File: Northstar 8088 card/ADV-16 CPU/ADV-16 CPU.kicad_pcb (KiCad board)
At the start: 2 copper layers, 228.1 x 165.3 mm, 111 parts, among them J1 Power In, J2 Conn_01x16_Socket, J3 Conn_01x18_Socket, P1 northstar card edge, Q1 2N3904, U1 74LS175, U10 74LS155, U11 74LS373, U12 8088-2, U13 74LS00, U14 74LS04, U15 74LS393, U16 74S08, U17 8284, U18 74LS258, U19 74LS174, U2 74S112, U20 74LS03, U21 74LS153, U22 74LS74, U23 74S00, U24 74LS393, U25 74LS244, U26 74LS258, U27 6309-1, U28 74LS373, U29 74LS245, U3 85ns_Delay, U30 74LS244, U31 74LS10, U32 4164, U33 4164, U34 4164, U35 4164, U36 4164, U37 4164, U38 4164, U39 4164, U4 74S04, U40 4164, U41 74LS280, U42 74LS374, U43 74LS373, U44 74LS138, U5 74LS32, U6 74LS74, U7 74LS20, U8 74LS74, U9 74LS00, Y1 24MHz

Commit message: more routing
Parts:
- moved R5 12.7 mm to (53.3, 121.9), turned to -90 degrees
- moved R14 12.7 mm to (95.2, 128.3), turned to -90 degrees
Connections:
- C2 pad 2: Net-(J2-Pin_2) -> GND
- J2 pad 2: Net-(J2-Pin_2) -> GND
- J2 pad 3: Net-(J2-Pin_2) -> GND
- J2 pad 4: Net-(J2-Pin_2) -> GND
- R1 pad 1: Net-(U17-X1) -> Net-(U17-X2)
- R2 pad 1: Net-(U17-X2) -> Net-(U17-X1)
- Y1 pad 1: Net-(U17-X2) -> Net-(U17-X1)
- Y1 pad 2: Net-(U17-X1) -> Net-(U17-X2)
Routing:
- net GND: track 544.1 -> 1816.6 mm, vias 2 -> 6
- net +5V: track 585.3 -> 1688.6 mm, vias 4 -> 7
- net /BDTR: track 0.00 -> 473.9 mm, vias 0 -> 5
- net PUP2: track 0.00 -> 325.4 mm, vias 0 -> 3
- net /WRT COMM: track 0.00 -> 324.4 mm, vias 0 -> 5
- net Net-(U1-~{Q0}): track 0.00 -> 306.5 mm, vias 0 -> 2
- net /page 2/PARITY: track 77.4 -> 358.6 mm, vias 3 -> 5
- net /BIO RES: track 0.00 -> 270.6 mm, vias 0 -> 3
- net /page 2/RAM OK: track 0.00 -> 255.1 mm, vias 0 -> 3
- net Net-(U1-Q2): track 0.00 -> 252.0 mm, vias 0 -> 2
- net /RD COMM: track 0.00 -> 249.7 mm, vias 0 -> 4
- net Net-(U6A-~{R}): track 0.00 -> 229.8 mm, vias 0 -> 2
- net Net-(U43-LE): track 0.00 -> 208.0 mm, vias 0 -> 2
- net Net-(U16-Pad10): track 0.00 -> 207.7 mm, vias 0 -> 2
- net Net-(U18-S): track 0.00 -> 191.2 mm, vias 0 -> 4
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- added copper zone on F.Cu, net GND

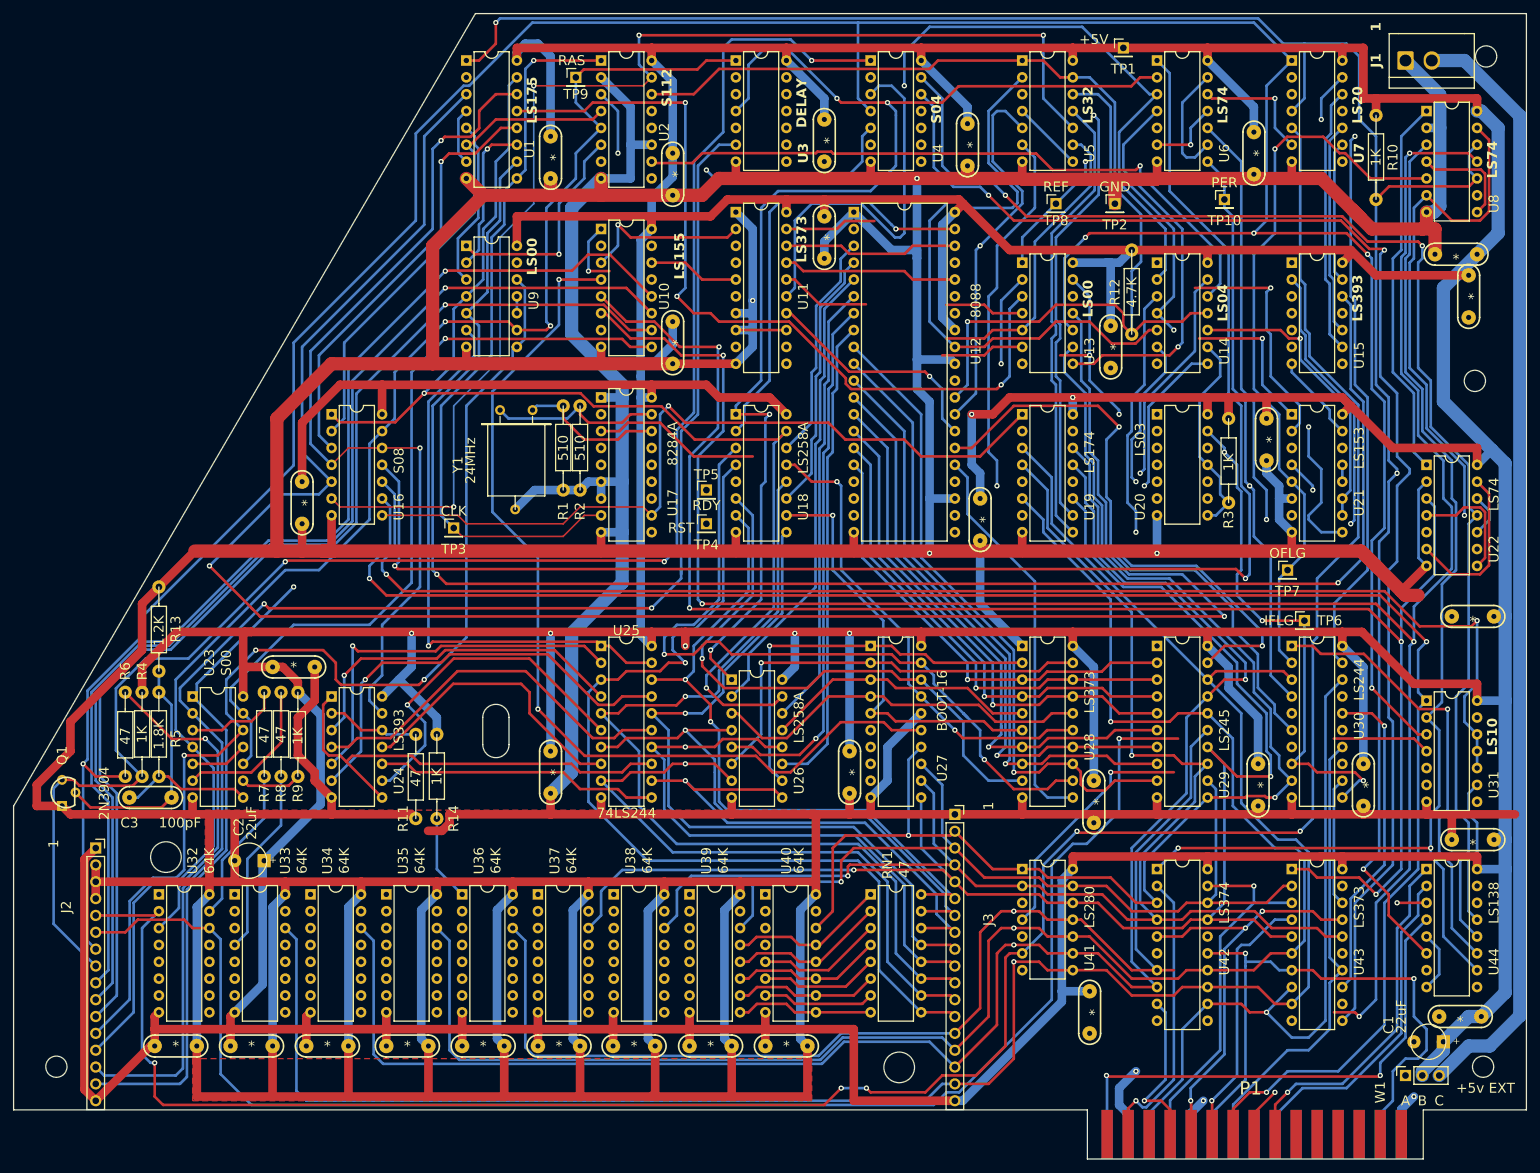
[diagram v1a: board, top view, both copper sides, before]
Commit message: finished layout, adding another diagnostic card extender
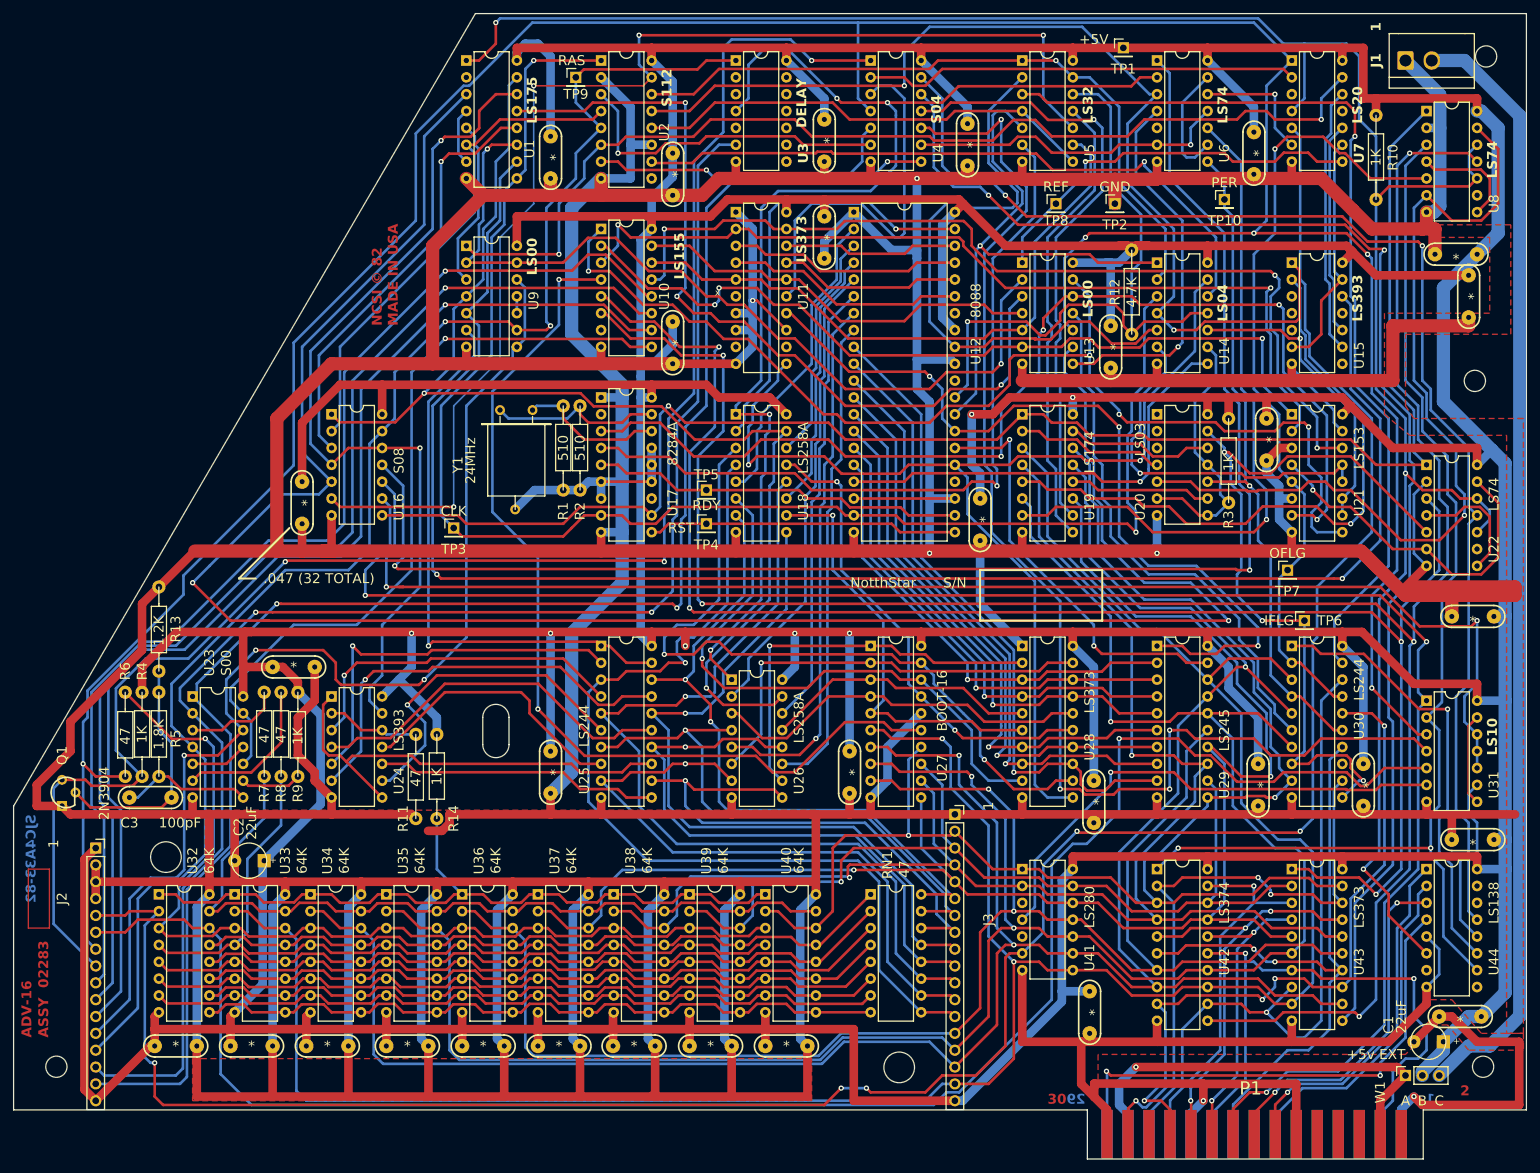
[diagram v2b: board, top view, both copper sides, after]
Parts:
- added G***: LOGO, Evan's parts:OSHW gear, B.Cu at (87.6, 60.3)
- added G***: LOGO, Evan's parts:Evan Logo, B.Cu at (228.0, 176.5)
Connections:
- Y1 pad 3: (no net) -> GND
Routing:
- net GND: track 1816.6 -> 2157.8 mm
- net Net-(U31-Pad4): track 14.8 -> 191.4 mm, vias 0 -> 4
- net /page 2/CAS ENABLE: track 98.9 -> 253.9 mm, vias 1 -> 3
- net Net-(U17-~{AEN1}): track 25.5 -> 166.0 mm, vias 0 -> 4
- net A16: track 13.8 -> 141.2 mm, vias 0 -> 3
- net Net-(U2A-~{Q}): track 41.3 -> 157.2 mm
- net UPMEM: track 59.4 -> 173.6 mm
- net RAM_AD0: track 19.0 -> 118.8 mm
- net /page 2/RFSH: track 13.0 -> 112.7 mm
- net RAM_AD2: track 17.9 -> 117.5 mm
- net /page 2//CAS: track 23.7 -> 123.3 mm
- net /page 2//RAS: track 28.3 -> 127.9 mm
- net RAM_AD1: track 16.9 -> 116.3 mm
- net /page 2//WRT: track 48.1 -> 147.2 mm
- net D1: track 261.7 -> 357.5 mm, vias 2 -> 3
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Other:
- board text added: ".047 (32 TOTAL)"
- board text added: "2"
- board text added: "29"
- board text added: "30"
- board text added: "ADV-16"
- board text added: "ASSY 02283"
- board text added: "NCSI © 82 MADE IN USA"
- board text added: "NotthStar"
- board text added: "S/N"
- board text added: "SJC4A33-82"
- board text added: "abzman2k.wordpress.com"
- board text added: "x"

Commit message: tweaks for production
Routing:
- net Net-(U16-Pad10): track 208.9 -> 208.3 mm
- net Net-(U1-~{Q0}): track 313.2 -> 312.5 mm
- net PUP2: track 339.4 -> 338.8 mm
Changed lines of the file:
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@@
     (fp_line (start 10.27 4.05) (end 10.27 -3.95)
       (stroke (width 0.1) (type solid)) (layer "F.Fab"))
-    (pad "1" thru_hole roundrect (at 0 0) (size 2.46 2.8) (drill 1.8) (layers "*.Cu" "*.Mask") (roundrect_rratio 0.101626)
+    (pad "1" thru_hole roundrect (at 0 0) (size 2.46 2.8) (drill 1.8) (layers "*.Cu" "*.Mask") (roundrect_rratio 0.1016260163)
       (net 2 "GND") (pinfunction "Pin_1") (pintype "passive"))
     (pad "2" thru_hole oval (at 3.96 0) (size 2.46 2.8) (drill 1.8) (layers "*.Cu" "*.Mask")
@@
   (via (at 104.14 20.955) (size 0.8) (drill 0.4) (layers "F.Cu" "B.Cu") (net 41))
   (via (at 234.95 148.59) (size 0.8) (drill 0.4) (layers "F.Cu" "B.Cu") (net 41))
-  (segment (start 238.76 106.515) (end 238.36 106.915) (width 0.4) (layer "B.Cu") (net 41))
   (segment (start 252.095 97.79) (end 254 95.885) (width 0.4) (layer "B.Cu") (net 41))
   (segment (start 254 95.885) (end 254 94.615) (width 0.4) (layer "B.Cu") (net 41))
@@
   (segment (start 217.805 90.805) (end 219.075 92.075) (width 0.4) (layer "B.Cu") (net 59))
   (segment (start 58.42 105.41) (end 64.135 111.125) (width 0.4) (layer "F.Cu") (net 61))
-  (segment (start 69.215 111.125) (end 69.85 111.125) (width 0.4) (layer "F.Cu") (net 61))
   (segment (start 69.85 111.125) (end 214.63 111.125) (width 0.4) (layer "F.Cu") (net 61))
   (segment (start 64.135 111.125) (end 69.85 111.125) (width 0.4) (layer "F.Cu") (net 61))
@@
   (segment (start 243.425 111.98) (end 251.24 111.98) (width 0.4) (layer "F.Cu") (net 162))
   (segment (start 90.17 106.045) (end 87.63 106.045) (width 0.4) (layer "F.Cu") (net 162))
-  (segment (start 89.535 106.045) (end 90.17 106.045) (width 0.4) (layer "F.Cu") (net 162))
   (segment (start 90.17 106.045) (end 237.49 106.045) (width 0.4) (layer "F.Cu") (net 162))
   (segment (start 251.24 111.98) (end 252.095 111.125) (width 0.4) (layer "F.Cu") (net 162))

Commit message: small updates to boards
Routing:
- net /page 2//REF RAS: track 172.0 -> 189.8 mm
- net /BDTR: track 475.5 -> 476.3 mm
- net Net-(Q1-B): track 35.9 -> 35.2 mm
